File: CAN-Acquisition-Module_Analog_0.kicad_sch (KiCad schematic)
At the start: 25 parts

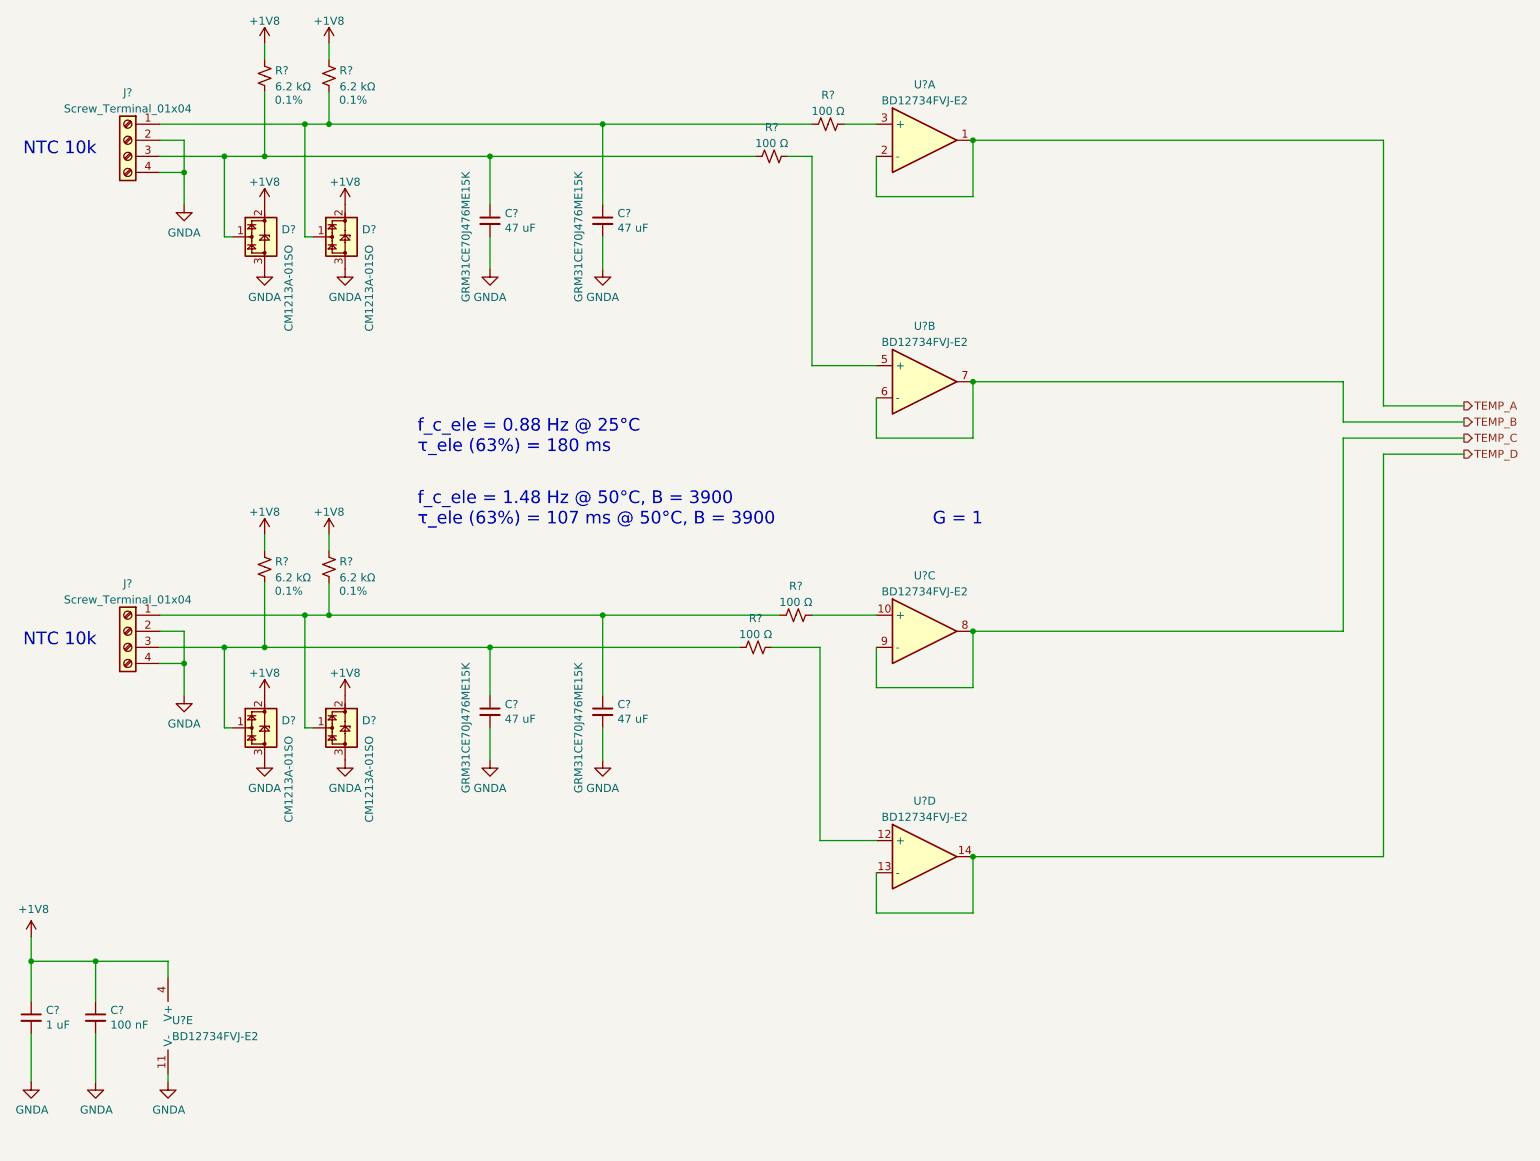
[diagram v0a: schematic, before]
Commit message: Added screen sections and annotations
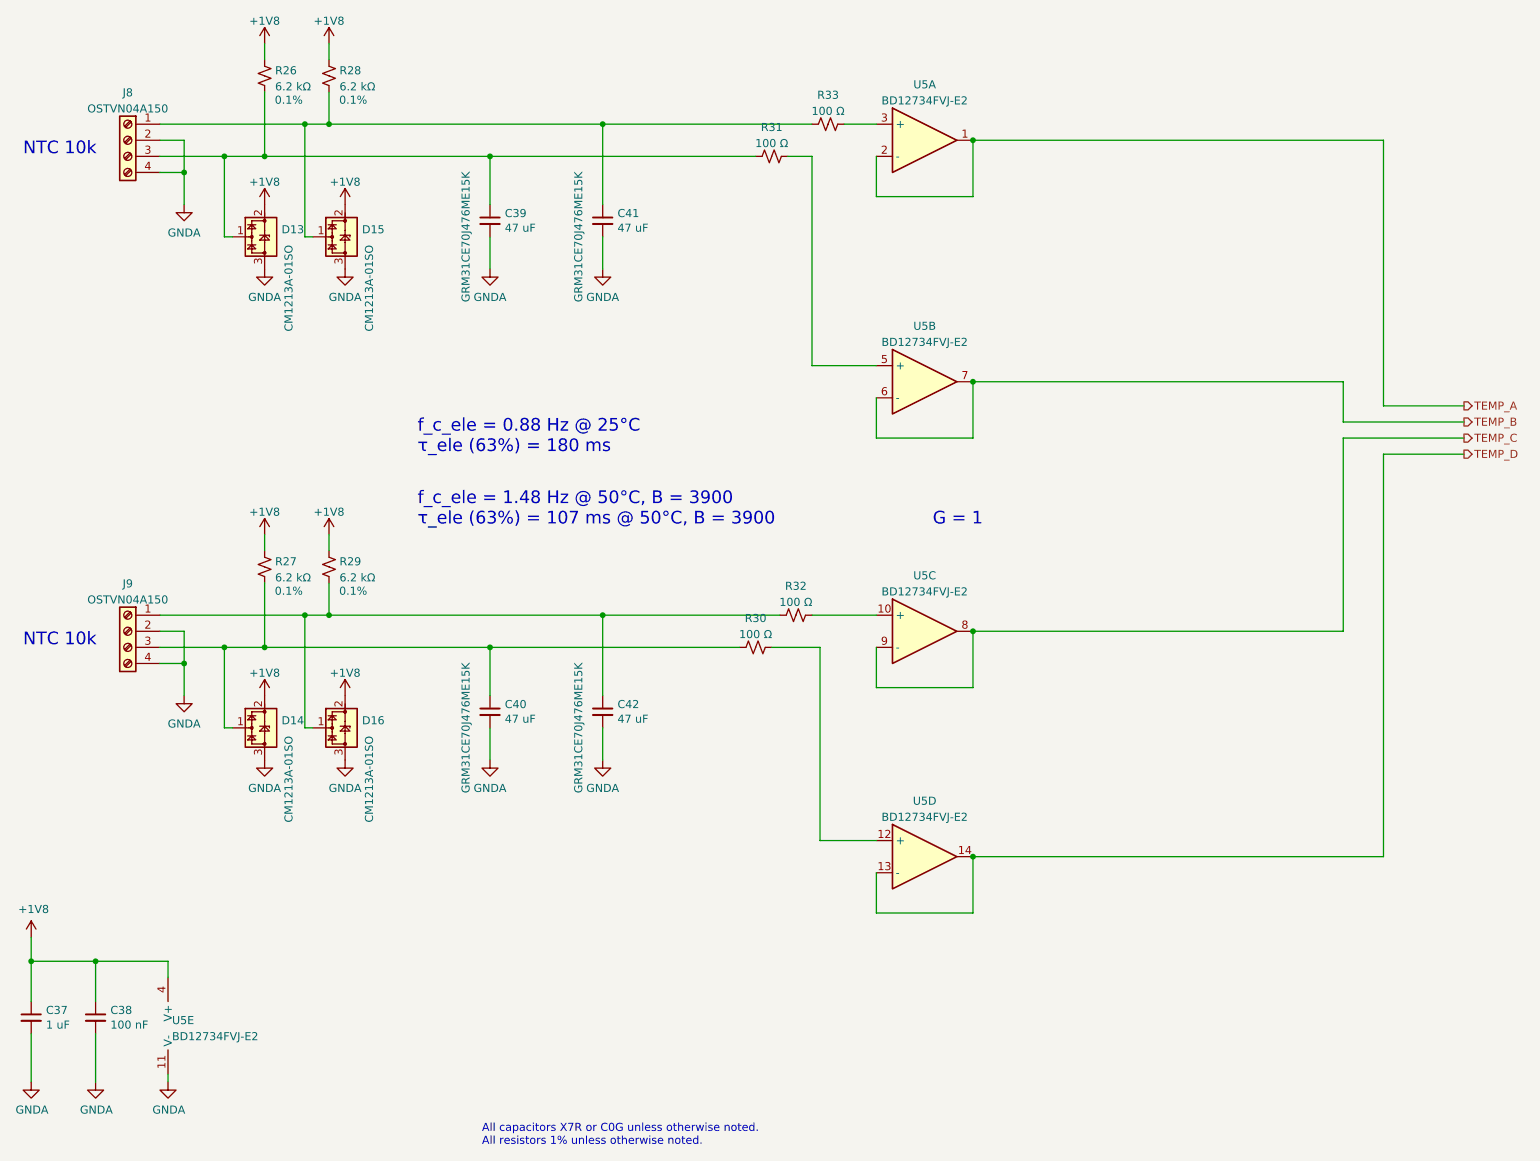
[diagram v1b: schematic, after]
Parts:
- removed C?: 100 nF, Capacitor_SMD:C_0402_1005Metric, symbol Device:C_Small
- removed C?: 1 uF, Capacitor_SMD:C_0603_1608Metric, symbol Device:C_Small
- removed D? (x4): CM1213A-01SO, Package_TO_SOT_SMD:SOT-23, symbol Power_Protection:CM1213A-01SO
- removed J? (x2): Screw_Terminal_01x04, CAN-Acquisition-Module:OSTVN04A150, symbol Connector:Screw_Terminal_01x04
- added C37: 1 uF, Capacitor_SMD:C_0603_1608Metric, symbol Device:C_Small
- added C38: 100 nF, Capacitor_SMD:C_0402_1005Metric, symbol Device:C_Small
- added D13, D14, D15, D16: CM1213A-01SO, Package_TO_SOT_SMD:SOT-23, symbol Power_Protection:CM1213A-01SO
- added J8, J9: OSTVN04A150, CAN-Acquisition-Module:OSTVN04A150, symbol Connector:Screw_Terminal_01x04
- gave numbers to parts that had none: 13
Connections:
- net +1V8: now also C37.1, C38.1, D13.2 (VP), D14.2 (VP), D15.2 (VP), D16.2 (VP)
- net GNDA: now also C37.2, C38.2, D13.3 (VN), D14.3 (VN), D15.3 (VN), D16.3 (VN), J8.2 (Pin_2), J8.4 (Pin_4), J9.2 (Pin_2), J9.4 (Pin_4)
- net at C39.1, R26.2, R31.2: now also D13.1 (CH1), J8.3 (Pin_3)
- net at C40.1, R27.2, R30.2: now also D14.1 (CH1), J9.3 (Pin_3)
- net at C41.1, R28.2, R33.2: now also D15.1 (CH1), J8.1 (Pin_1)
- net at C42.1, R29.2, R32.2: now also D16.1 (CH1), J9.1 (Pin_1)
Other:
- note added: "All capacitors X7R or C0G unless otherwise noted. All resistors 1% unless otherwise noted."

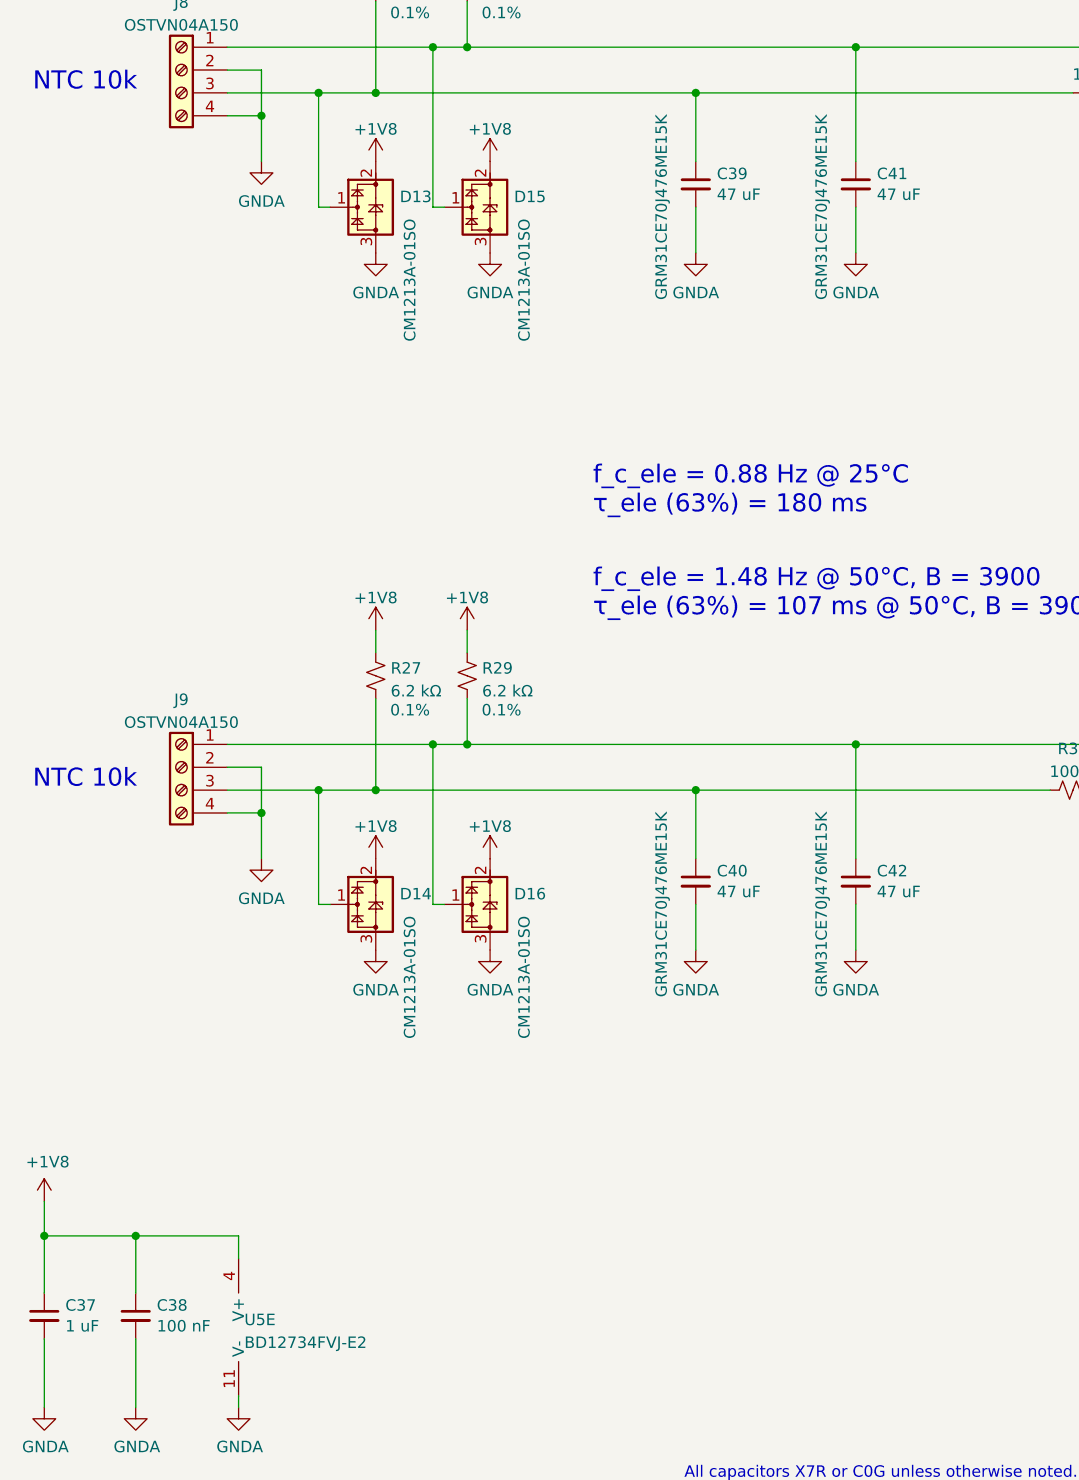
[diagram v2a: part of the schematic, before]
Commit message: Layout of analog section started
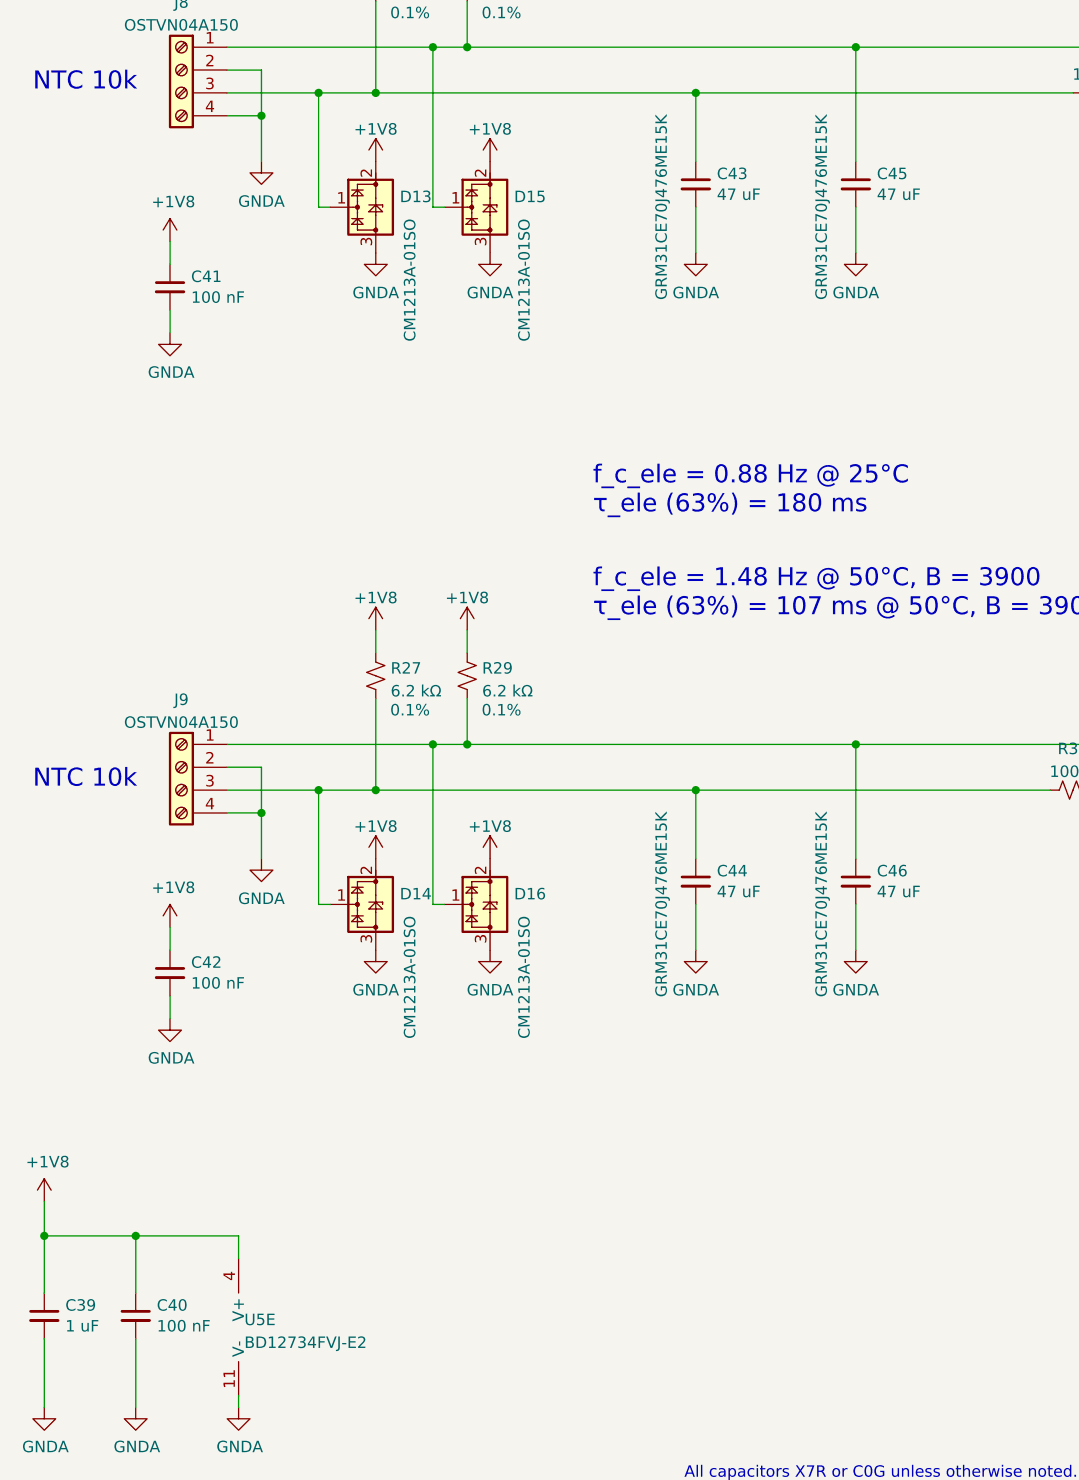
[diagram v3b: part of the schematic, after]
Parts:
- added C41, C42: 100 nF, Capacitor_SMD:C_0402_1005Metric, symbol Device:C_Small
- renumbered C37 to C39, C38 to C40, C39 to C43, C40 to C44, C41 to C45, C42 to C46
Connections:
- net +1V8: now also C41.1, C42.1
- net GNDA: now also C41.2, C42.2

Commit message: Finished power outputs
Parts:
- renumbered C39 to C38, C40 to C39, C41 to C40, C42 to C41, C43 to C42, C44 to C43, C45 to C44, C46 to C45, D13 to D15, D14 to D16, D15 to D17, D16 to D18, R26 to R27, R27 to R28, R28 to R29, R29 to R30, R30 to R31, R31 to R32, R32 to R33, R33 to R34

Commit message: forgor to save
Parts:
- renumbered C38 to C39, C39 to C40, C40 to C41, C41 to C42, C42 to C43, C43 to C44, C44 to C45, C45 to C46

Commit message: Rev. A1 release
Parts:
- renumbered C39 to C40, C40 to C41, C41 to C42, C42 to C43, C43 to C44, C44 to C45, C45 to C46, C46 to C47, R27 to R29, R28 to R30, R29 to R31, R30 to R32, R31 to R33, R32 to R34, R33 to R35, R34 to R36, U5 to U6
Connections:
- net TEMP_A: now also U6.6 (-), U6.7; no longer U6.1, U6.2 (-)
- net TEMP_B: now also U6.1, U6.2 (-); no longer U6.6 (-), U6.7
- net TEMP_C: now also U6.13 (-), U6.14; no longer U6.8, U6.9 (-)
- net TEMP_D: now also U6.8, U6.9 (-); no longer U6.13 (-), U6.14
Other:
- moved on the sheet: C42, C43, C44, C45, C46, C47, D15, D16, D17, D18, J8, J9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
